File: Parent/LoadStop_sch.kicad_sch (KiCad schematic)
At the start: 5 parts, among them K1 Y14x-1C-xxDS, Q9 NMOS

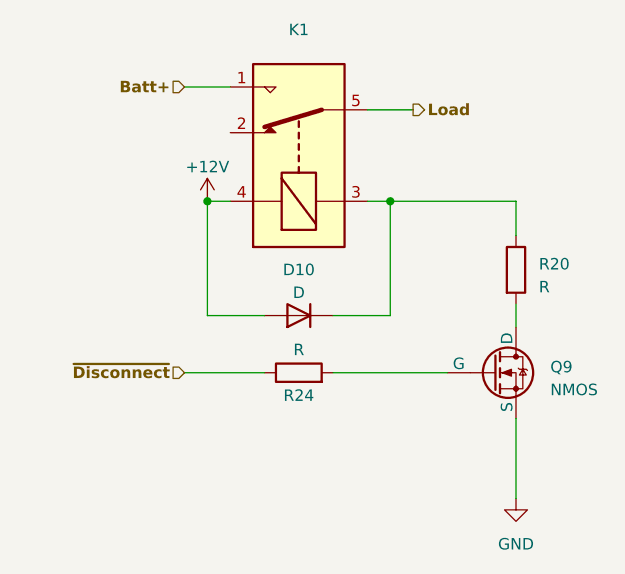
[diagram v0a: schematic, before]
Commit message: Updated Parent - Moved workspace to cloud
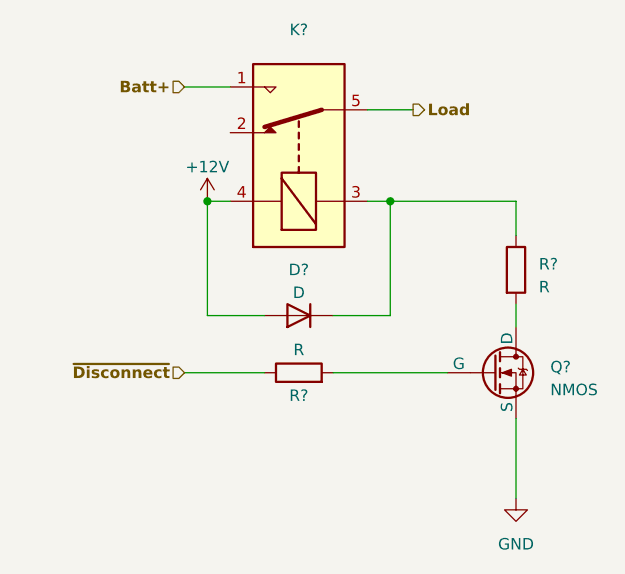
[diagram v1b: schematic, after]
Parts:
- renumbered D10 to D?, K1 to K?, Q9 to Q?, R20 to R?, R24 to R?
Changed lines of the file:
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@@
   (symbol (lib_id "Device:R") (at 66.04 45.72 0) (unit 1)
     (in_bom yes) (on_board yes) (dnp no) (fields_autoplaced)
-    (property "Reference" "R20" (at 68.58 45.085 0)
+    (property "Reference" "R?" (at 68.58 45.085 0)
       (effects (font (size 1.27 1.27)) (justify left))
     )
@@
       (project "Parent"
         (path "/1451ec1d-c665-471b-ba41-1d89ef6a63bf/0387320d-a4dd-4eff-b26e-da29a9485b5e"
-          (reference "R20") (unit 1)
-        )
-        (path "/1451ec1d-c665-471b-ba41-1d89ef6a63bf/d4f99db8-9696-41dc-a8b6-d8395b75e8ba"
-          (reference "R70") (unit 1)
+          (reference "R?") (unit 1)
+        )
+        (path "/1451ec1d-c665-471b-ba41-1d89ef6a63bf/d4f99db8-9696-41dc-a8b6-d8395b75e8ba"
+          (reference "R?") (unit 1)
         )
       )
@@
   (symbol (lib_id "Device:R") (at 41.91 57.15 90) (unit 1)
     (in_bom yes) (on_board yes) (dnp no)
-    (property "Reference" "R24" (at 41.91 59.69 90)
+    (property "Reference" "R?" (at 41.91 59.69 90)
       (effects (font (size 1.27 1.27)))
     )
@@
       (project "Parent"
         (path "/1451ec1d-c665-471b-ba41-1d89ef6a63bf/0387320d-a4dd-4eff-b26e-da29a9485b5e"
-          (reference "R24") (unit 1)
-        )
-        (path "/1451ec1d-c665-471b-ba41-1d89ef6a63bf/d4f99db8-9696-41dc-a8b6-d8395b75e8ba"
-          (reference "R29") (unit 1)
+          (reference "R?") (unit 1)
+        )
+        (path "/1451ec1d-c665-471b-ba41-1d89ef6a63bf/d4f99db8-9696-41dc-a8b6-d8395b75e8ba"
+          (reference "R?") (unit 1)
         )
       )
@@
   (symbol (lib_id "power:GND") (at 66.04 71.12 0) (unit 1)
     (in_bom yes) (on_board yes) (dnp no) (fields_autoplaced)
-    (property "Reference" "#PWR031" (at 66.04 77.47 0)
+    (property "Reference" "#PWR?" (at 66.04 77.47 0)
       (effects (font (size 1.27 1.27)) hide)
     )
@@
       (project "Parent"
         (path "/1451ec1d-c665-471b-ba41-1d89ef6a63bf/0387320d-a4dd-4eff-b26e-da29a9485b5e"
-          (reference "#PWR031") (unit 1)
-        )
-        (path "/1451ec1d-c665-471b-ba41-1d89ef6a63bf/d4f99db8-9696-41dc-a8b6-d8395b75e8ba"
-          (reference "#PWR032") (unit 1)
+          (reference "#PWR?") (unit 1)
+        )
+        (path "/1451ec1d-c665-471b-ba41-1d89ef6a63bf/d4f99db8-9696-41dc-a8b6-d8395b75e8ba"
+          (reference "#PWR?") (unit 1)
         )
       )
@@
   (symbol (lib_id "Relay:Y14x-1C-xxDS") (at 41.91 33.02 90) (unit 1)
     (in_bom yes) (on_board yes) (dnp no) (fields_autoplaced)
-    (property "Reference" "K1" (at 41.91 19.05 90)
+    (property "Reference" "K?" (at 41.91 19.05 90)
       (effects (font (size 1.27 1.27)))
     )
@@
       (project "Parent"
         (path "/1451ec1d-c665-471b-ba41-1d89ef6a63bf"
-          (reference "K1") (unit 1)
-        )
-        (path "/1451ec1d-c665-471b-ba41-1d89ef6a63bf/0387320d-a4dd-4eff-b26e-da29a9485b5e"
-          (reference "K2") (unit 1)
-        )
-        (path "/1451ec1d-c665-471b-ba41-1d89ef6a63bf/d4f99db8-9696-41dc-a8b6-d8395b75e8ba"
-          (reference "K1") (unit 1)
+          (reference "K?") (unit 1)
+        )
+        (path "/1451ec1d-c665-471b-ba41-1d89ef6a63bf/0387320d-a4dd-4eff-b26e-da29a9485b5e"
+          (reference "K?") (unit 1)
+        )
+        (path "/1451ec1d-c665-471b-ba41-1d89ef6a63bf/d4f99db8-9696-41dc-a8b6-d8395b75e8ba"
+          (reference "K?") (unit 1)
         )
       )
@@
   (symbol (lib_id "power:+12V") (at 31.75 38.1 0) (unit 1)
     (in_bom yes) (on_board yes) (dnp no) (fields_autoplaced)
-    (property "Reference" "#PWR033" (at 31.75 41.91 0)
+    (property "Reference" "#PWR?" (at 31.75 41.91 0)
       (effects (font (size 1.27 1.27)) hide)
     )
@@
       (project "Parent"
         (path "/1451ec1d-c665-471b-ba41-1d89ef6a63bf/0387320d-a4dd-4eff-b26e-da29a9485b5e"
-          (reference "#PWR033") (unit 1)
-        )
-        (path "/1451ec1d-c665-471b-ba41-1d89ef6a63bf/d4f99db8-9696-41dc-a8b6-d8395b75e8ba"
-          (reference "#PWR034") (unit 1)
+          (reference "#PWR?") (unit 1)
+        )
+        (path "/1451ec1d-c665-471b-ba41-1d89ef6a63bf/d4f99db8-9696-41dc-a8b6-d8395b75e8ba"
+          (reference "#PWR?") (unit 1)
         )
       )
@@
   (symbol (lib_id "Device:D") (at 41.91 50.8 180) (unit 1)
     (in_bom yes) (on_board yes) (dnp no) (fields_autoplaced)
-    (property "Reference" "D10" (at 41.91 45.72 0)
+    (property "Reference" "D?" (at 41.91 45.72 0)
       (effects (font (size 1.27 1.27)))
     )
@@
       (project "Parent"
         (path "/1451ec1d-c665-471b-ba41-1d89ef6a63bf/0387320d-a4dd-4eff-b26e-da29a9485b5e"
-          (reference "D10") (unit 1)
-        )
-        (path "/1451ec1d-c665-471b-ba41-1d89ef6a63bf/d4f99db8-9696-41dc-a8b6-d8395b75e8ba"
-          (reference "D11") (unit 1)
+          (reference "D?") (unit 1)
+        )
+        (path "/1451ec1d-c665-471b-ba41-1d89ef6a63bf/d4f99db8-9696-41dc-a8b6-d8395b75e8ba"
+          (reference "D?") (unit 1)
         )
       )
@@
   (symbol (lib_id "Simulation_SPICE:NMOS") (at 63.5 57.15 0) (unit 1)
     (in_bom yes) (on_board yes) (dnp no) (fields_autoplaced)
-    (property "Reference" "Q9" (at 69.85 56.515 0)
+    (property "Reference" "Q?" (at 69.85 56.515 0)
       (effects (font (size 1.27 1.27)) (justify left))
     )
@@
       (project "Parent"
         (path "/1451ec1d-c665-471b-ba41-1d89ef6a63bf/d4f99db8-9696-41dc-a8b6-d8395b75e8ba"
-          (reference "Q9") (unit 1)
-        )
-        (path "/1451ec1d-c665-471b-ba41-1d89ef6a63bf/0387320d-a4dd-4eff-b26e-da29a9485b5e"
-          (reference "Q8") (unit 1)
-        )
-      )
+          (reference "Q?") (unit 1)
+        )
+        (path "/1451ec1d-c665-471b-ba41-1d89ef6a63bf/0387320d-a4dd-4eff-b26e-da29a9485b5e"
+          (reference "Q?") (unit 1)
+        )
+      )
